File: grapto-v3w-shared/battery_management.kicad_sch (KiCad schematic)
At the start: 19 parts

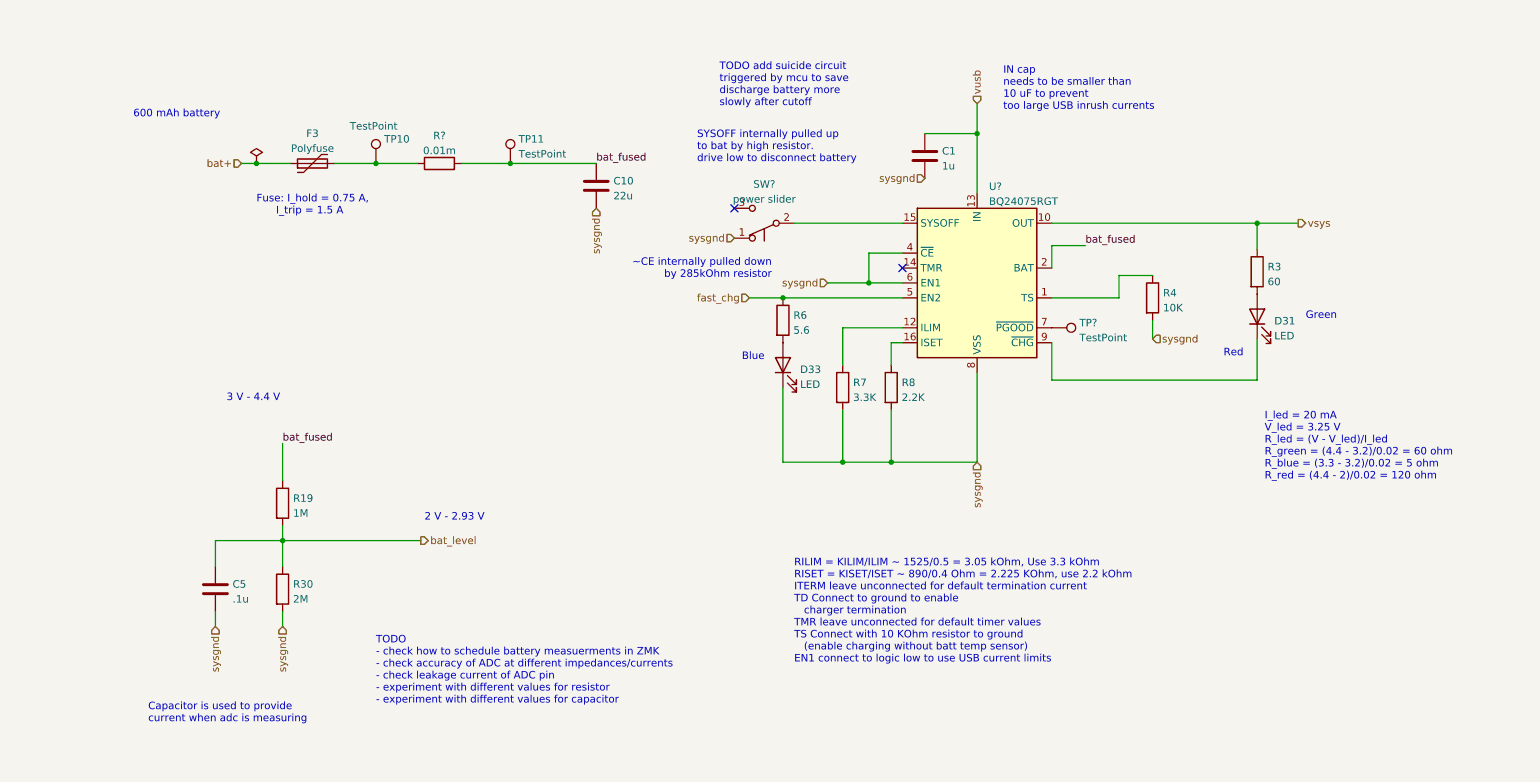
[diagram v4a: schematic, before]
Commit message: Added footprints.
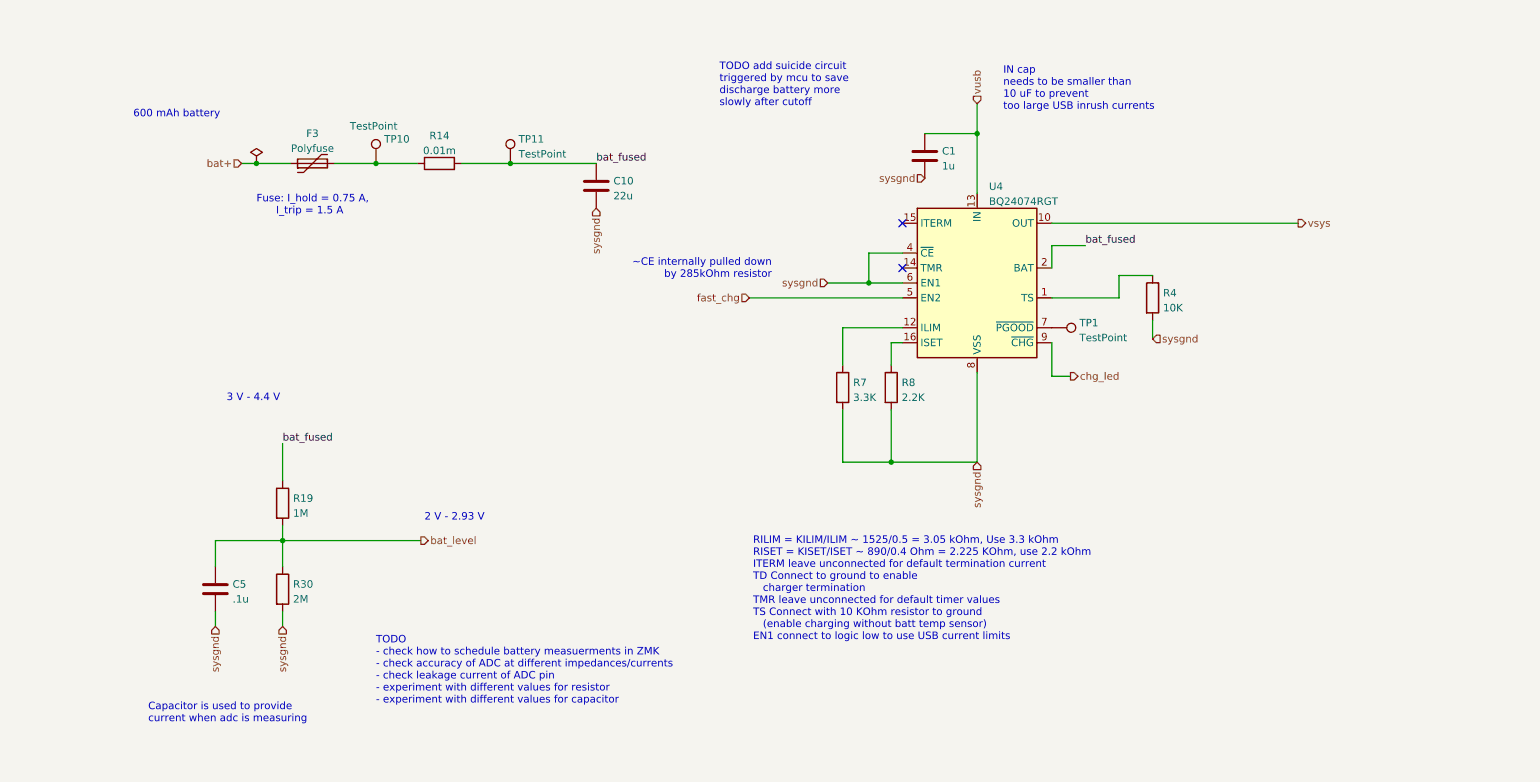
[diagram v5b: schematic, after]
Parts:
- removed D31, D33: LED, LED_SMD:LED_0805_2012Metric_Pad1.15x1.40mm_HandSolder, symbol Device:LED
- removed R3: 60, Resistor_SMD:R_0603_1608Metric_Pad0.98x0.95mm_HandSolder, symbol Device:R
- removed R6: 5.6, Resistor_SMD:R_0603_1608Metric_Pad0.98x0.95mm_HandSolder, symbol Device:R
- removed SW?: power slider, symbol Switch:SW_Push_SPDT
- removed U?: BQ24075RGT, Package_DFN_QFN:VQFN-16-1EP_3x3mm_P0.5mm_EP1.6x1.6mm, symbol Battery_Management:BQ24075RGT
- added U4: BQ24074RGT, Package_DFN_QFN:VQFN-16-1EP_3x3mm_P0.5mm_EP1.6x1.6mm, symbol Battery_Management:BQ24074RGT
- C1: footprint Fuse:Fuse_0603_1608Metric_Pad1.05x0.95mm_HandSolder -> LED_SMD:LED_1210_3225Metric_Pad1.42x2.65mm_HandSolder
- R14: renamed from R?; footprint (none) -> Resistor_SMD:R_0603_1608Metric_Pad0.98x0.95mm_HandSolder
- gave numbers to parts that had none: 1
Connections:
- net bat_fused: now also U4.2 (BAT), U4.3 (BAT)
- net fast_chg: now also U4.5 (EN2)
- net sysgnd: now also U4.17 (VSS), U4.4 (~{CE}), U4.6 (EN1), U4.8 (VSS)
- net vsys: now also U4.10 (OUT), U4.11 (OUT)
- net vusb: now also U4.13 (IN)
- net at R4.1: now also U4.1 (TS)
- net at R7.1: now also U4.12 (ILIM)
- net at R8.1: now also U4.16 (ISET)
- net at TP1.1: now also U4.7 (~{PGOOD})
- new net chg_led: U4.9 (~{CHG})
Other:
- note removed: "Blue"
- note removed: "Green"
- note removed: "I_led = 20 mA V_led = 3.25 V R_led = (V - V_led)/I_led R_green = (4.4 - 3.2)/0.02 = 60 ohm R_blue = (3.3 - 3.2)/0.02 = 5 ohm R_red = (4.4 - 2)/0.02 = 120 ohm"
- note removed: "Red"
- note removed: "SYSOFF internally pulled up to bat by high resistor. drive low to disconnect battery"

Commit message: before adding hotswaps
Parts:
- C1: footprint LED_SMD:LED_1210_3225Metric_Pad1.42x2.65mm_HandSolder -> Capacitor_SMD:C_0603_1608Metric_Pad1.08x0.95mm_HandSolder
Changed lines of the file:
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@@
       (effects (font (size 1.27 1.27)) (justify left))
     )
-    (property "Footprint" "LED_SMD:LED_1210_3225Metric_Pad1.42x2.65mm_HandSolder" (id 2) (at 179.4002 57.15 0)
+    (property "Footprint" "Capacitor_SMD:C_0603_1608Metric_Pad1.08x0.95mm_HandSolder" (id 2) (at 179.4002 57.15 0)
       (effects (font (size 1.27 1.27)) hide)
     )

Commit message: left half pcb draft.
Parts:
- removed U4: BQ24074RGT, Package_DFN_QFN:VQFN-16-1EP_3x3mm_P0.5mm_EP1.6x1.6mm, symbol Battery_Management:BQ24074RGT
- added SW31: SW_SPDT, grapto-v3w:SW_SK-3296S-01-L2, symbol Switch:SW_SPDT
- added U4: BQ24075RGT, Package_DFN_QFN:VQFN-16-1EP_3x3mm_P0.5mm_EP1.6x1.6mm, symbol Battery_Management:BQ24075RGT
- R19: value 1M -> 1M2
- R30: value 2M -> 3M
- TP1, TP10, TP11: footprint grapto-v3w:TestPoint_THTPad_D2.0mm_Drill1.0mm -> Connector_PinHeader_2.54mm:PinHeader_1x01_P2.54mm_Vertical
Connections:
- net bat_fused: now also U4.2 (BAT), U4.3 (BAT)
- net chg_led: now also U4.9 (~{CHG})
- net fast_chg: now also U4.5 (EN2)
- net sysgnd: now also SW31.1 (A), U4.17 (VSS), U4.4 (~{CE}), U4.6 (EN1), U4.8 (VSS)
- net vsys: now also U4.10 (OUT), U4.11 (OUT)
- net vusb: now also U4.13 (IN)
- net at R4.1: now also U4.1 (TS)
- net at R8.1: now also U4.16 (ISET)
- net at R7.1: now also U4.12 (ILIM)
- net at TP1.1: now also U4.7 (~{PGOOD})
- new net: SW31.2 (B), U4.15 (SYSOFF)
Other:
- note added: "2.14 V - 3.00 V"
- note added: "3 V - 4.2 V"
- note added: "Battery Connected"
- note added: "Fuse: I_hold = 0.5 A"
- note added: "Sysoff has internal 5 MOhm pullup"
- note removed: "2 V - 2.93 V"
- note removed: "3 V - 4.4 V"
- note removed: "Fuse: I_hold = 0.75 A, I_trip = 1.5 A"

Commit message: Right pcb almost finished.
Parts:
- C10: footprint Fuse:Fuse_0603_1608Metric_Pad1.05x0.95mm_HandSolder -> Capacitor_SMD:C_0603_1608Metric_Pad1.08x0.95mm_HandSolder
- R19: value 1M2 -> 1M
- R30: value 3M -> 2M
- TP1, TP10, TP11: footprint Connector_PinHeader_2.54mm:PinHeader_1x01_P2.54mm_Vertical -> TestPoint:TestPoint_THTPad_D2.0mm_Drill1.0mm
